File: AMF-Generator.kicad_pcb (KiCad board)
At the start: 4 copper layers, 70 x 75 mm, 59 parts, among them J1 SW_OUT, J2 CUR_SENSE, J3 PWR_IN, J4 I2C_5V, J5 I2C_3V3, Q1 ISC012N04LM6ATMA1, Q2 ISC012N04LM6ATMA1, U1 ACS732KLATR-75AB, U2 UCC21540, U3 LTC1968, U4 LT1880, U5 CAT3200-5, U6 NLSX4373DR2G, U7 ADC101C021CIMK, U9 QTPY

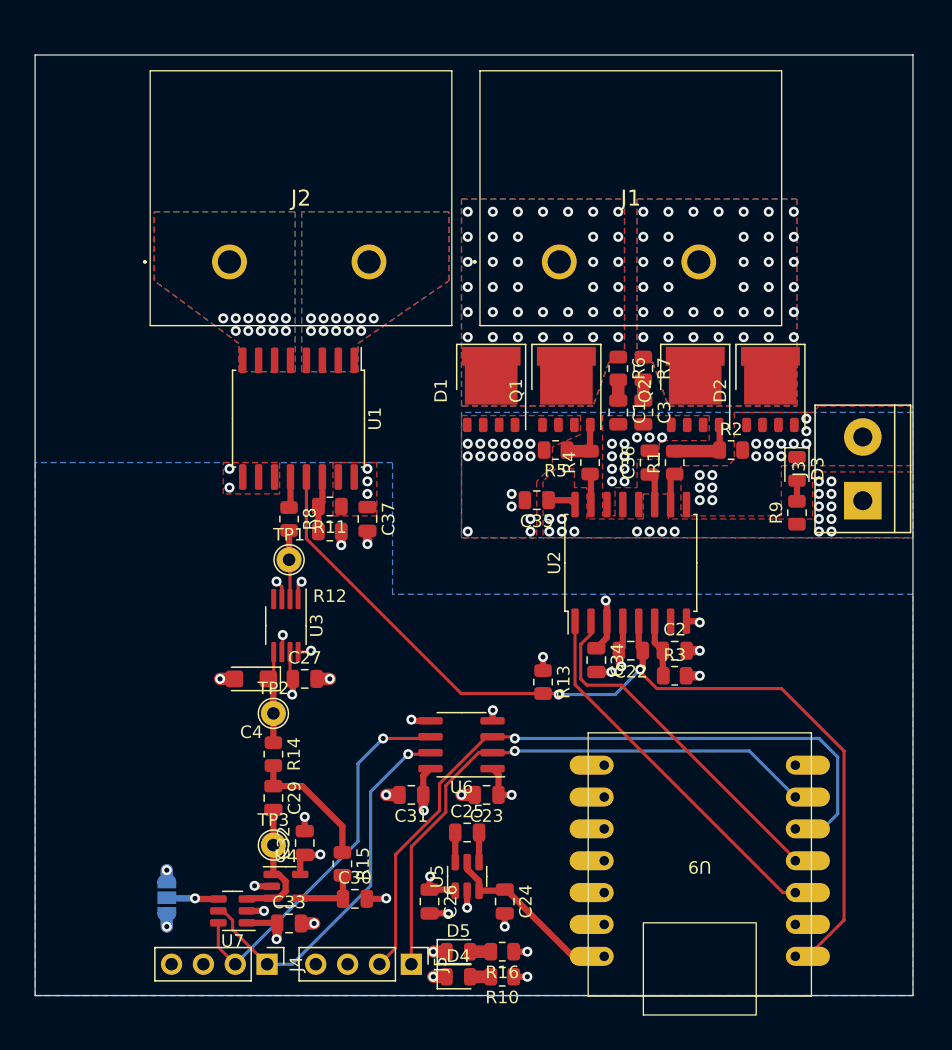
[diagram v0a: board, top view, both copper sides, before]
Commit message: Cleanup, changed board outline, DRC errors resolved
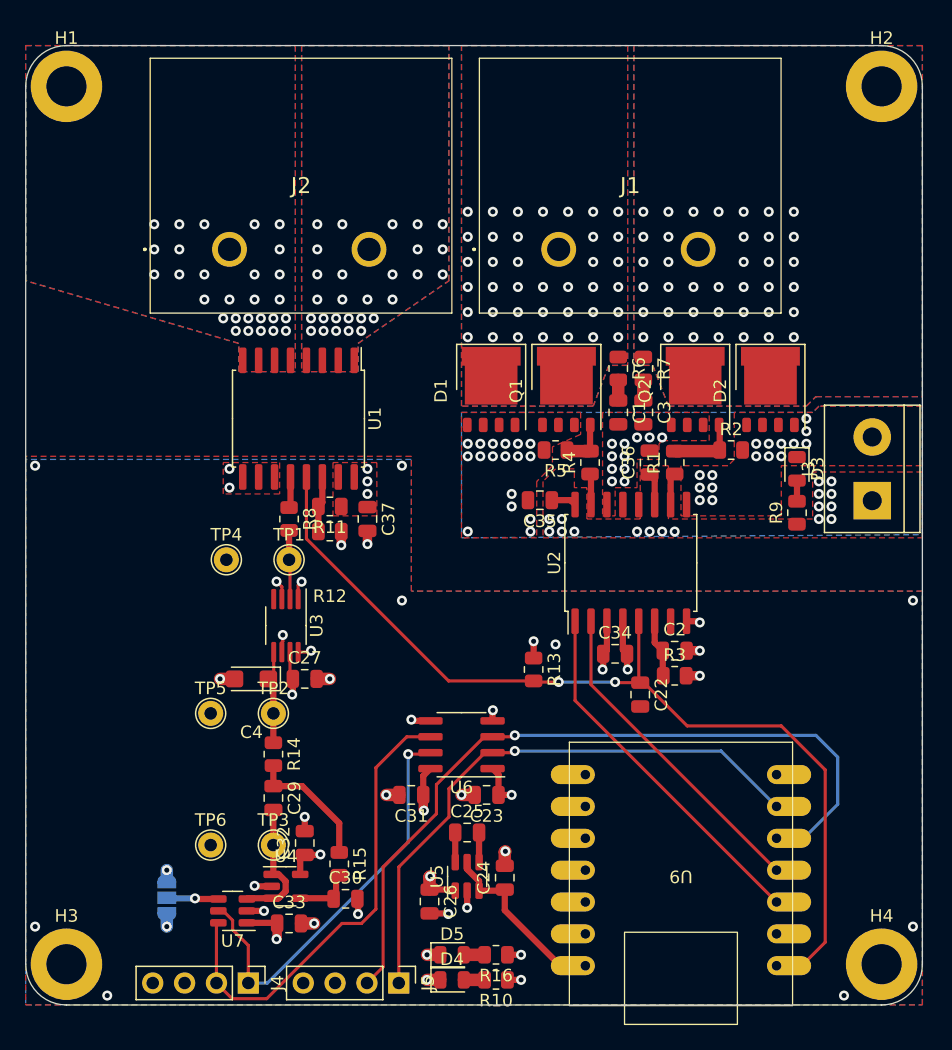
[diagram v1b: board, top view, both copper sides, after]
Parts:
- added H1: MountingHole, MountingHole:MountingHole_3.2mm_M3_ISO7380_Pad, F.Cu at (98.0, 22.0)
- added H2: MountingHole, MountingHole:MountingHole_3.2mm_M3_ISO7380_Pad, F.Cu at (163.0, 22.0)
- added H3: MountingHole, MountingHole:MountingHole_3.2mm_M3_ISO7380_Pad, F.Cu at (98.0, 92.0)
- added H4: MountingHole, MountingHole:MountingHole_3.2mm_M3_ISO7380_Pad, F.Cu at (163.0, 92.0)
- added TP4: TestPoint, TestPoint:TestPoint_THTPad_D2.0mm_Drill1.0mm, F.Cu at (110.8, 59.8)
- added TP5: TestPoint, TestPoint:TestPoint_THTPad_D2.0mm_Drill1.0mm, F.Cu at (109.5, 72.0)
- added TP6: TestPoint, TestPoint:TestPoint_THTPad_D2.0mm_Drill1.0mm, F.Cu at (109.5, 82.5)
- moved C22 3.58 mm to (143.8, 70.5), turned to -90 degrees
- moved J4 2.12 mm to (112.5, 93.5)
- moved C24 1.90 mm to (132.9, 85.1), turned to 90 degrees
- moved J5 1.80 mm to (124.5, 93.5)
- moved U9 1.68 mm to (147.0, 84.5)
- moved C34 1.58 mm to (141.8, 67.2), turned to 0 degrees
- moved R13 1.25 mm to (135.2, 68.5)
- moved J1 1.00 mm to (137.2, 35.0)
- moved J2 1.00 mm to (111.0, 35.0)
- moved C30 0.75 mm to (120.2, 86.8)
- moved J3 0.75 mm to (162.2, 55.0)
- moved D4 0.56 mm to (128.8, 93.2)
- moved D5 0.56 mm to (128.8, 91.2)
- moved R10 0.56 mm to (132.2, 93.2)
- moved R16 0.56 mm to (132.2, 91.2)
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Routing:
- net SDA_5: track 30.6 -> 37.5 mm, vias 1 -> 0
- net FAULT: track 79.2 -> 75.3 mm
- net Net-(#FLG03-pwr): track 14.9 -> 12.5 mm
- net SCL_5: track 30.5 -> 32.7 mm
- net PWM_B: track 28.1 -> 26.0 mm
- net GND: track 33.5 -> 32.3 mm, vias 28 -> 36
- net Net-(U3-VOUT): track 7.57 -> 6.40 mm
- net Net-(U4--IN): track 5.33 -> 4.44 mm
- net +12V: track 4.82 -> 4.57 mm, vias 19 -> 17
- net SW_B: vias 36 -> 38
- net SW_A: vias 36 -> 38
- net AC_B: vias 11 -> 28
- net AC_A: vias 11 -> 28
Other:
- board size 70 x 75 mm -> 71.5 x 76.5 mm

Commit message: More warnings resolved
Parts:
- moved D5 0.25 mm to (128.8, 91.0)
- moved R16 0.25 mm to (132.2, 91.0)

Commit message: Lots of vias
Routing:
- net SCL_5: track 32.7 -> 34.7 mm
- net SW_B: vias 38 -> 137
- net SW_A: vias 38 -> 86
- net AC_B: vias 28 -> 95
- net AC_A: vias 28 -> 64

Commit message: adding useful labels
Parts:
- moved J3 1.00 mm to (161.2, 55.0)
- moved D4 0.50 mm to (129.2, 93.2)
- moved D5 0.50 mm to (129.2, 91.0)
- moved R10 0.50 mm to (132.8, 93.2)
- moved R16 0.50 mm to (132.8, 91.0)
- moved D3 0.25 mm to (156.0, 52.5)
- moved R9 0.25 mm to (156.0, 56.0)
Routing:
- net GNDPWR: vias 44 -> 43
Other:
- board text added: "+12V"
- board text added: "+5V"
- board text added: "3V"
- board text added: "3V3"
- board text added: "3V3 I2C"
- board text added: "5V"
- board text added: "5V I2C"
- board text added: "GND"
- board text added: "SCL"
- board text added: "SDA"

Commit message: More labels and cleanup
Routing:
- net FAULT: track 75.3 -> 74.7 mm
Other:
- board text added: "CURRENT SENSE"
- board text added: "SWITCHING"
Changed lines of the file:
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@@
     (property "ki_keywords" "capacitor cap")
     (attr smd)
-    (fp_text reference "C32" (at 3.0875 0.5 90) (layer "F.SilkS")
+    (fp_text reference "C32" (at 3.0875 1 90) (layer "F.SilkS")
         (effects (font (size 1 1) (thickness 0.15)))
     )
@@
   (gr_line (start 98 18.75) (end 163 18.75)
     (stroke (width 0.1) (type default)) (layer "Edge.Cuts"))
-  (gr_text "+12V" (at 165.25 56.5 -90) (layer "B.SilkS")
+  (gr_text "+12V" (at 164.25 56.5 -90) (layer "B.SilkS")
     (effects (font (size 0.8 0.8) (thickness 0.15)) (justify left bottom mirror))
   )
@@
     (effects (font (size 1 1) (thickness 0.15)) (justify left bottom mirror))
   )
-  (gr_text "GND" (at 165.25 51.25 -90) (layer "B.SilkS")
+  (gr_text "GND" (at 164.25 51.25 -90) (layer "B.SilkS")
     (effects (font (size 0.8 0.8) (thickness 0.15)) (justify left bottom mirror))
   )
@@
     (effects (font (size 0.8 0.8) (thickness 0.15)) (justify left bottom))
   )
+  (gr_text "SWITCHING" (at 157.75 35 90) (layer "F.SilkS")
+    (effects (font (size 1 1) (thickness 0.15)) (justify left bottom))
+  )
   (gr_text "+5V" (at 106 92) (layer "F.SilkS")
     (effects (font (size 0.8 0.8) (thickness 0.15)) (justify left bottom))
@@
     (effects (font (size 0.8 0.8) (thickness 0.15)) (justify left bottom))
   )
+  (gr_text "CURRENT SENSE" (at 102.5 34.75 90) (layer "F.SilkS")
+    (effects (font (size 1 1) (thickness 0.15)) (justify left bottom))
+  )
   (gr_text "SDA" (at 108.75 92) (layer "F.SilkS")
     (effects (font (size 0.8 0.8) (thickness 0.15)) (justify left bottom))
@@
   (segment (start 144.05 69.55) (end 147.5 73) (width 0.25) (layer "F.Cu") (net 17))
   (segment (start 137.25 69.5) (end 135.3375 69.5) (width 0.25) (layer "F.Cu") (net 17))
-  (segment (start 143.75 69.55) (end 144.05 69.55) (width 0.25) (layer "F.Cu") (net 17))
   (segment (start 141.8 69.55) (end 143.75 69.55) (width 0.25) (layer "F.Cu") (net 17))
   (segment (start 158.5 90.25) (end 156.63 92.12) (width 0.25) (layer "F.Cu") (net 17))
@@
   (segment (start 117.135 58.073173) (end 128.474327 69.4125) (width 0.25) (layer "F.Cu") (net 17))
   (segment (start 155 73) (end 158.5 76.5) (width 0.25) (layer "F.Cu") (net 17))
-  (segment (start 135.3375 69.5) (end 135.25 69.4125) (width 0.25) (layer "F.Cu") (net 17))
   (segment (start 143.635 69.435) (end 143.635 64.65) (width 0.25) (layer "F.Cu") (net 17))
   (segment (start 147.5 73) (end 155 73) (width 0.25) (layer "F.Cu") (net 17))
-  (segment (start 143.75 69.55) (end 143.635 69.435) (width 0.25) (layer "F.Cu") (net 17))
   (via (at 137.25 69.5) (size 0.8) (drill 0.4) (layers "F.Cu" "B.Cu") (net 17))
   (via (at 141.75 69.5) (size 0.8) (drill 0.4) (layers "F.Cu" "B.Cu") (net 17))
@@
       4b44a1d9-f7b2-4ed1-affc-8a051b094c8f
       51592da7-5a05-466d-aecf-9ff220fdef48
-      580e6cb7-3279-44d5-993d-5ef4c5ebc7e8
       62d9ea48-b1ec-4e43-91a1-bfd589a32376
       6ebcf974-3cc6-46f8-aae1-463f5665e4f2
@@
       e22f0d89-402e-495f-aeac-960b2467ddbf
       e8c0f29b-6551-4198-8da2-a9a62d69014d
-      f11c8e90-508e-41cf-9c4f-aea9d3af6830
       fd4e7c6f-1e2a-4f64-a786-0167e60635f1
       fdd41ff4-aadd-48e8-b1fd-72ed46a22761

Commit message: Updated with selectable I2C addresses
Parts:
- U7: value ADC101C021CIMK -> ADC101C027CIMK
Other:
- board text added: "(FLOAT)"
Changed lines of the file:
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@@
         (effects (font (size 1 1) (thickness 0.15)))
     )
-    (fp_text value "ADC101C021CIMK" (at 0 2.4) (layer "F.Fab")
+    (fp_text value "ADC101C027CIMK" (at 0 2.4) (layer "F.Fab")
         (effects (font (size 1 1) (thickness 0.15)))
     )
@@
     (property "ki_keywords" "Solder Jumper SPDT")
     (attr exclude_from_pos_files)
-    (fp_text reference "JP2" (at 0 1.8 -270) (layer "B.SilkS")
+    (fp_text reference "JP2" (at -4.45 0 -270) (layer "B.SilkS")
         (effects (font (size 1 1) (thickness 0.15)) (justify mirror))
     )
@@
     (effects (font (size 0.8 0.8) (thickness 0.15)) (justify left bottom mirror))
   )
+  (gr_text "GND" (at 104.25 89) (layer "B.SilkS")
+    (effects (font (size 1 1) (thickness 0.15)) (justify left bottom mirror))
+  )
   (gr_text "3V3 I2C" (at 123.75 90.75) (layer "B.SilkS")
     (effects (font (size 1 1) (thickness 0.15)) (justify left bottom mirror))
@@
     (effects (font (size 0.8 0.8) (thickness 0.15)) (justify left bottom mirror))
   )
+  (gr_text "(FLOAT)" (at 104.25 87.25) (layer "B.SilkS")
+    (effects (font (size 1 1) (thickness 0.15)) (justify left bottom mirror))
+  )
+  (gr_text "+5V" (at 104.5 85.5) (layer "B.SilkS")
+    (effects (font (size 1 1) (thickness 0.15)) (justify left bottom mirror))
+  )
   (gr_text "+5V" (at 108.75 92) (layer "B.SilkS")

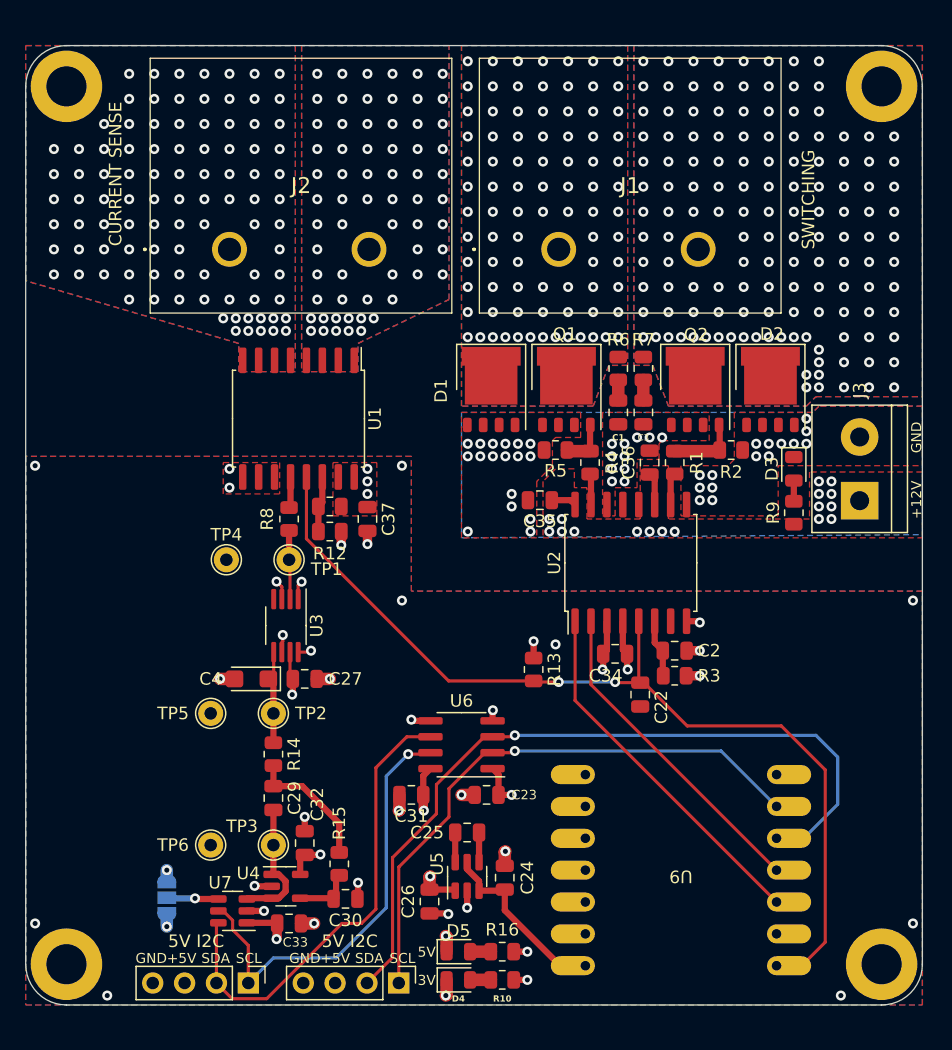
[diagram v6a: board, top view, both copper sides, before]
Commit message: Fix schematic issues (incl QTPY symbol) and some board cleanup
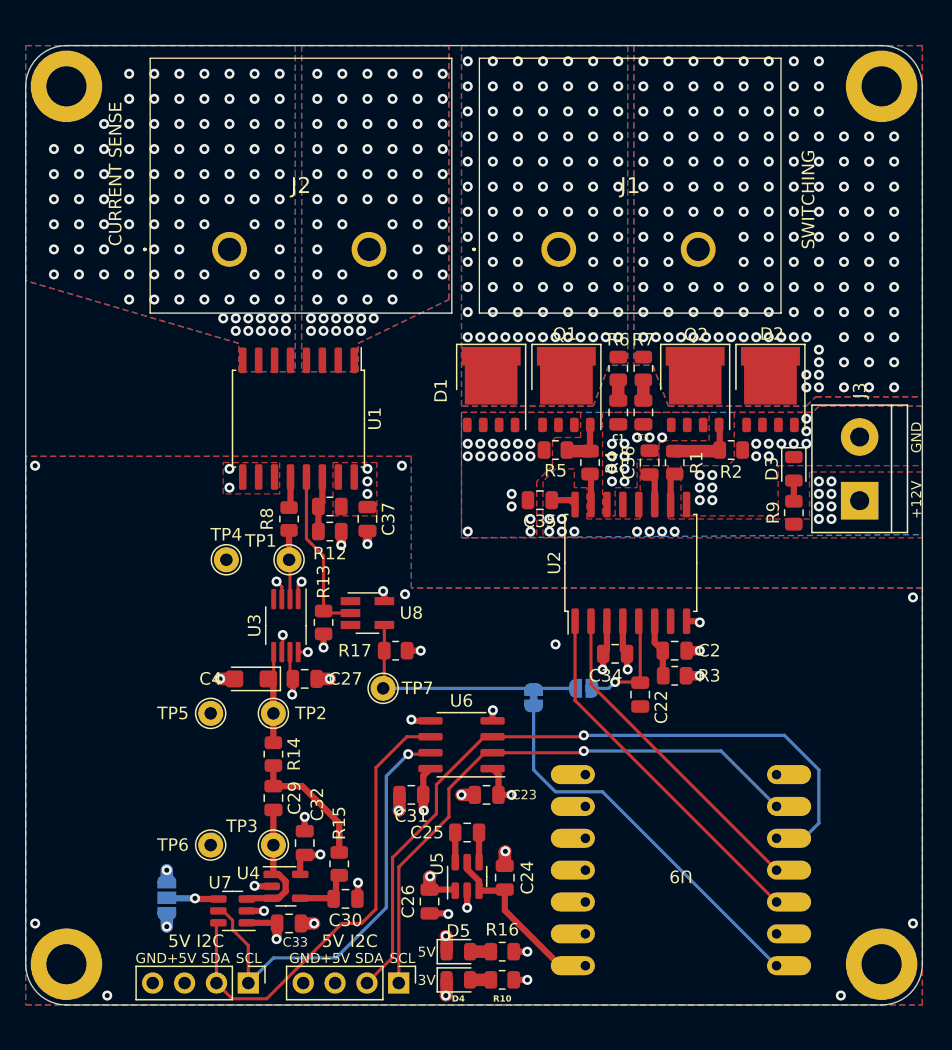
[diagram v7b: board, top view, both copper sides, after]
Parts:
- added JP1: Driver-Disable, Jumper:SolderJumper-2_P1.3mm_Open_RoundedPad1.0x1.5mm, B.Cu at (139.2, 70.0)
- added JP3: MCU_Disable, Jumper:SolderJumper-2_P1.3mm_Bridged_RoundedPad1.0x1.5mm, B.Cu at (135.2, 70.8)
- added R17: 1K, Resistor_SMD:R_0805_2012Metric, F.Cu at (124.2, 67.0)
- added TP7: TestPoint, TestPoint:TestPoint_THTPad_D2.0mm_Drill1.0mm, F.Cu at (123.2, 70.0)
- added U8: 74LVC1G06, Package_TO_SOT_SMD:SOT-23-5_HandSoldering, F.Cu at (122.0, 64.0)
- moved R13 17.2 mm to (118.5, 64.8), turned to 90 degrees
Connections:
- C22 pad 1: FAULT -> Net-(JP1-B)
- R13 pad 1: +3V3 -> +5V
- R13 pad 2: FAULT -> Net-(U1-~{FAULT})
- U1 pad 13: FAULT -> Net-(U1-~{FAULT})
- U2 pad 5: FAULT -> Net-(JP1-B)
- U9 pad 1: FAULT -> Net-(JP3-B)
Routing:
- net FAULT: track 74.7 -> 20.5 mm, vias 2 -> 0
- net Net-(JP3-B): track 0.00 -> 30.9 mm
- net Net-(U1-~{FAULT}): track 0.00 -> 13.5 mm
- net Net-(JP1-B): track 0.00 -> 8.84 mm, vias 0 -> 1
- net SDA_3V3: track 59.0 -> 56.3 mm
- net +5V: track 18.5 -> 20.5 mm, vias 10 -> 12

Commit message: misc changes
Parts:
- moved C34 0.05 mm to (141.8, 67.2)
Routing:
- net GND: vias 36 -> 65
